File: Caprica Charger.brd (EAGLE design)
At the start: 160 x 100 mm, 60 parts, among them J1 POWER_JACKPTH, Q4 MOSFET, Q5 MOSFET

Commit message: Everything patched together
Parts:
- moved R11 20.5 mm to (8.89, 5.08)
- moved D2 16.5 mm to (12.7, 6.35), turned to 0 degrees
- moved R13 11.7 mm to (21.6, 5.08)
- moved U$5 10.8 mm to (5.71, 11.3), turned to 0 degrees
- moved D4 8.89 mm to (24.1, 6.35), turned to 0 degrees
- moved R12 8.03 mm to (29.2, 5.08)
- moved D3 2.54 mm to (34.3, 6.35), turned to 0 degrees
- moved R10 1.67 mm to (19.4, 9.40), turned to 180 degrees
- moved R9 0.25 mm to (21.1, 11.8)
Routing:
- net VIN: track 42.2 -> 61.3 mm
- net N$10: track 12.7 -> 29.6 mm, vias 0 -> 2
- net THERM: track 6.38 -> 19.2 mm
- net N$12: track 8.86 -> 16.1 mm
- net N$13: track 1.57 -> 3.62 mm
- net N$11: track 7.00 -> 8.67 mm
- net N$1: track 1.57 -> 2.37 mm
- net GND: vias 18 -> 19
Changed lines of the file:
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@@
 <layer number="23" name="tOrigins" color="15" fill="1" visible="yes" active="yes"/>
 <layer number="24" name="bOrigins" color="15" fill="1" visible="yes" active="yes"/>
-<layer number="25" name="tNames" color="7" fill="1" visible="yes" active="yes"/>
-<layer number="26" name="bNames" color="7" fill="1" visible="yes" active="yes"/>
-<layer number="27" name="tValues" color="7" fill="1" visible="yes" active="yes"/>
-<layer number="28" name="bValues" color="7" fill="1" visible="yes" active="yes"/>
+<layer number="25" name="tNames" color="7" fill="1" visible="no" active="yes"/>
+<layer number="26" name="bNames" color="7" fill="1" visible="no" active="yes"/>
+<layer number="27" name="tValues" color="7" fill="1" visible="no" active="yes"/>
+<layer number="28" name="bValues" color="7" fill="1" visible="no" active="yes"/>
 <layer number="29" name="tStop" color="7" fill="3" visible="no" active="yes"/>
 <layer number="30" name="bStop" color="7" fill="6" visible="no" active="yes"/>
@@
 <element name="C9" library="SparkFun" package="1206" value="10uF" x="55.88" y="6.35" rot="R270"/>
 <element name="C4" library="SparkFun" package="1206" value="2.2uF" x="39.37" y="5.08" rot="R90"/>
-<element name="D2" library="SparkFun" package="LED-1206" value="" x="29.21" y="6.35" rot="R90"/>
-<element name="D3" library="SparkFun" package="LED-1206" value="" x="36.83" y="6.35" rot="R90"/>
-<element name="D4" library="SparkFun" package="LED-1206" value="" x="33.02" y="6.35" rot="R90"/>
-<element name="R11" library="Taylor" package="0603-RES" value="100k" x="29.21" y="2.54" rot="R270"/>
-<element name="R12" library="Taylor" package="0603-RES" value="100k" x="36.83" y="2.54" rot="R270"/>
-<element name="R13" library="Taylor" package="0603-RES" value="100k" x="33.02" y="2.54" rot="R270"/>
+<element name="D2" library="SparkFun" package="LED-1206" value="" x="12.7" y="6.35"/>
+<element name="D3" library="SparkFun" package="LED-1206" value="" x="34.29" y="6.35"/>
+<element name="D4" library="SparkFun" package="LED-1206" value="" x="24.13" y="6.35"/>
+<element name="R11" library="Taylor" package="0603-RES" value="100k" x="8.89" y="5.08" rot="R270"/>
+<element name="R12" library="Taylor" package="0603-RES" value="100k" x="29.21" y="5.08" rot="R270"/>
+<element name="R13" library="Taylor" package="0603-RES" value="100k" x="21.59" y="5.08" rot="R270"/>
 <element name="C1" library="Taylor" package="0603-CAP" value="0.1uF" x="24.13" y="9.525" rot="R90"/>
 <element name="R16" library="Taylor" package="0603-RES" value="100k" x="21.082" y="10.414" rot="R180"/>
-<element name="R9" library="Taylor" package="0603-RES" value="9.31k" x="21.082" y="11.557" rot="R180"/>
-<element name="R10" library="Taylor" package="0603-RES" value="430k" x="21.082" y="9.144"/>
+<element name="R9" library="Taylor" package="0603-RES" value="9.31k" x="21.082" y="11.811" rot="R180"/>
+<element name="R10" library="Taylor" package="0603-RES" value="430k" x="19.431" y="9.398" rot="R180"/>
 <element name="CTTC" library="Taylor" package="0603-CAP" value="0.056uF" x="35.56" y="12.7" rot="R180"/>
 <element name="R7" library="Taylor" package="0603-RES" value="100k" x="43.18" y="3.81" rot="R180"/>
@@
 <element name="C19" library="SparkFun" package="1206" value="10uF" x="29.21" y="25.4" rot="R90"/>
 <element name="C20" library="SparkFun" package="1206" value="10uF" x="26.67" y="25.4" rot="R90"/>
-<element name="U$5" library="Taylor" package="DF13-2" value="DF13-2HORIZONTAL" x="16.383" y="9.525" rot="R270"/>
+<element name="U$5" library="Taylor" package="DF13-2" value="DF13-2HORIZONTAL" x="5.715" y="11.303"/>
 </elements>
 <signals>
@@
 <via x="41.148" y="7.747" extent="1-16" drill="0.4064"/>
 <wire x1="38.1" y1="16.51" x2="37.465" y2="15.875" width="0.254" layer="1"/>
+<via x="43.688" y="18.415" extent="1-16" drill="0.4064"/>
 </signal>
 <signal name="VIN">
@@
 <vertex x="16.383" y="19.304"/>
 </polygon>
-<wire x1="33.02" y1="1.8" x2="36.83" y2="1.8" width="0.4064" layer="1"/>
-<wire x1="36.83" y1="1.8" x2="29.21" y2="1.8" width="0.4064" layer="1"/>
+<wire x1="21.59" y1="4.34" x2="29.21" y2="4.34" width="0.4064" layer="1"/>
+<wire x1="29.21" y1="4.34" x2="8.89" y2="4.34" width="0.4064" layer="1"/>
 <wire x1="17.04" y1="25.4" x2="16.51" y2="24.87" width="0.6096" layer="1"/>
 <wire x1="16.51" y1="24.87" x2="16.51" y2="22.86" width="0.6096" layer="1"/>
-<wire x1="29.21" y1="1.8" x2="26.14" y2="1.8" width="0.4064" layer="1"/>
-<wire x1="26.14" y1="1.8" x2="21.59" y2="6.35" width="0.4064" layer="1"/>
-<via x="21.59" y="6.35" extent="1-16" drill="0.4064"/>
-<wire x1="21.59" y1="6.35" x2="21.59" y2="8.89" width="0.4064" layer="16"/>
-<wire x1="21.59" y1="8.89" x2="15.24" y2="15.24" width="0.4064" layer="16"/>
+<wire x1="8.89" y1="4.34" x2="19.79" y2="4.34" width="0.4064" layer="1"/>
+<wire x1="19.79" y1="4.34" x2="20.32" y2="7.62" width="0.4064" layer="1"/>
+<via x="20.32" y="7.62" extent="1-16" drill="0.4064"/>
+<wire x1="20.32" y1="7.62" x2="20.32" y2="8.89" width="0.4064" layer="16"/>
+<wire x1="20.32" y1="8.89" x2="15.24" y2="15.24" width="0.4064" layer="16"/>
 <wire x1="15.24" y1="15.24" x2="15.24" y2="17.78" width="0.4064" layer="16"/>
 <wire x1="15.24" y1="17.78" x2="13.7" y2="19.32" width="0.4064" layer="16"/>
@@
 <via x="30.607" y="14.351" extent="1-16" drill="0.4064"/>
 <wire x1="30.607" y1="14.351" x2="30.607" y2="14.986" width="0.254" layer="1"/>
-<wire x1="21.822" y1="11.557" x2="22.584" y2="11.557" width="0.4064" layer="1"/>
+<wire x1="21.822" y1="11.811" x2="22.584" y2="11.557" width="0.4064" layer="1"/>
 <wire x1="22.584" y1="11.557" x2="22.987" y2="11.938" width="0.4064" layer="1"/>
 <via x="22.987" y="11.938" extent="1-16" drill="0.4064"/>
@@
 <contactref element="D2" pad="A"/>
 <contactref element="R11" pad="1"/>
-<wire x1="29.21" y1="4.85" x2="29.21" y2="3.28" width="0.4064" layer="1"/>
+<wire x1="11.2" y1="6.35" x2="8.89" y2="5.82" width="0.4064" layer="1"/>
 </signal>
 <signal name="N$10">
@@
 <wire x1="33.528" y1="15.24" x2="32.131" y2="15.24" width="0.254" layer="1"/>
 <wire x1="32.131" y1="15.24" x2="31.75" y2="14.859" width="0.254" layer="1"/>
-<wire x1="29.21" y1="7.85" x2="29.21" y2="11.43" width="0.254" layer="1"/>
 <wire x1="29.21" y1="11.43" x2="31.75" y2="13.97" width="0.254" layer="1"/>
 <wire x1="31.75" y1="13.97" x2="31.75" y2="14.859" width="0.254" layer="1"/>
+<wire x1="29.21" y1="11.43" x2="27.94" y2="10.16" width="0.3048" layer="1"/>
+<wire x1="27.94" y1="10.16" x2="27.94" y2="8.89" width="0.3048" layer="1"/>
+<via x="27.94" y="8.89" extent="1-16" drill="0.4064"/>
+<via x="16.51" y="8.89" extent="1-16" drill="0.4064"/>
+<wire x1="16.51" y1="8.89" x2="13.97" y2="6.35" width="0.3048" layer="1"/>
+<wire x1="14.2" y1="6.35" x2="13.97" y2="6.35" width="0.3048" layer="1"/>
+<wire x1="27.94" y1="8.89" x2="25.4" y2="6.35" width="0.3048" layer="16"/>
+<wire x1="25.4" y1="6.35" x2="19.05" y2="6.35" width="0.3048" layer="16"/>
+<wire x1="19.05" y1="6.35" x2="16.51" y2="8.89" width="0.3048" layer="16"/>
 </signal>
 <signal name="N$11">
@@
 <wire x1="37.85" y1="14.46" x2="37.85" y2="10.664" width="0.254" layer="1"/>
 <wire x1="37.85" y1="10.664" x2="37.846" y2="10.541" width="0.254" layer="1"/>
-<wire x1="36.83" y1="7.85" x2="36.83" y2="9.398" width="0.254" layer="1"/>
+<wire x1="35.79" y1="6.35" x2="36.83" y2="9.398" width="0.254" layer="1"/>
 <wire x1="36.83" y1="9.398" x2="37.846" y2="10.541" width="0.254" layer="1"/>
 </signal>
@@
 <wire x1="37.338" y1="14.448" x2="37.338" y2="11.938" width="0.254" layer="1"/>
 <wire x1="37.338" y1="11.938" x2="33.02" y2="7.62" width="0.254" layer="1"/>
-<wire x1="33.02" y1="7.62" x2="33.02" y2="7.85" width="0.254" layer="1"/>
+<wire x1="33.02" y1="7.62" x2="25.63" y2="6.35" width="0.254" layer="1"/>
 </signal>
 <signal name="N$13">
 <contactref element="D3" pad="A"/>
 <contactref element="R12" pad="1"/>
-<wire x1="36.83" y1="4.85" x2="36.83" y2="3.28" width="0.4064" layer="1"/>
+<wire x1="32.79" y1="6.35" x2="29.21" y2="5.82" width="0.4064" layer="1"/>
 </signal>
 <signal name="N$14">
 <contactref element="D4" pad="A"/>
 <contactref element="R13" pad="1"/>
-<wire x1="33.02" y1="4.85" x2="33.02" y2="3.28" width="0.4064" layer="1"/>
+<wire x1="22.63" y1="6.35" x2="21.59" y2="5.82" width="0.4064" layer="1"/>
 </signal>
 <signal name="THERM">
@@
 <contactref element="R16" pad="2"/>
 <contactref element="U$5" pad="P1"/>
-<wire x1="20.342" y1="11.557" x2="20.342" y2="10.414" width="0.6096" layer="1"/>
-<wire x1="20.342" y1="10.414" x2="20.342" y2="9.144" width="0.6096" layer="1"/>
-<wire x1="20.342" y1="11.557" x2="18.934" y2="11.695" width="0.4064" layer="1"/>
-<wire x1="18.934" y1="11.695" x2="16.383" y2="11.695" width="0.4064" layer="1"/>
+<wire x1="20.342" y1="11.811" x2="20.342" y2="10.414" width="0.6096" layer="1"/>
+<wire x1="20.342" y1="10.414" x2="20.171" y2="9.398" width="0.6096" layer="1"/>
+<wire x1="20.342" y1="11.811" x2="18.934" y2="11.695" width="0.4064" layer="1"/>
+<wire x1="18.934" y1="11.695" x2="3.545" y2="11.303" width="0.4064" layer="1"/>
 </signal>
 <signal name="N$18">

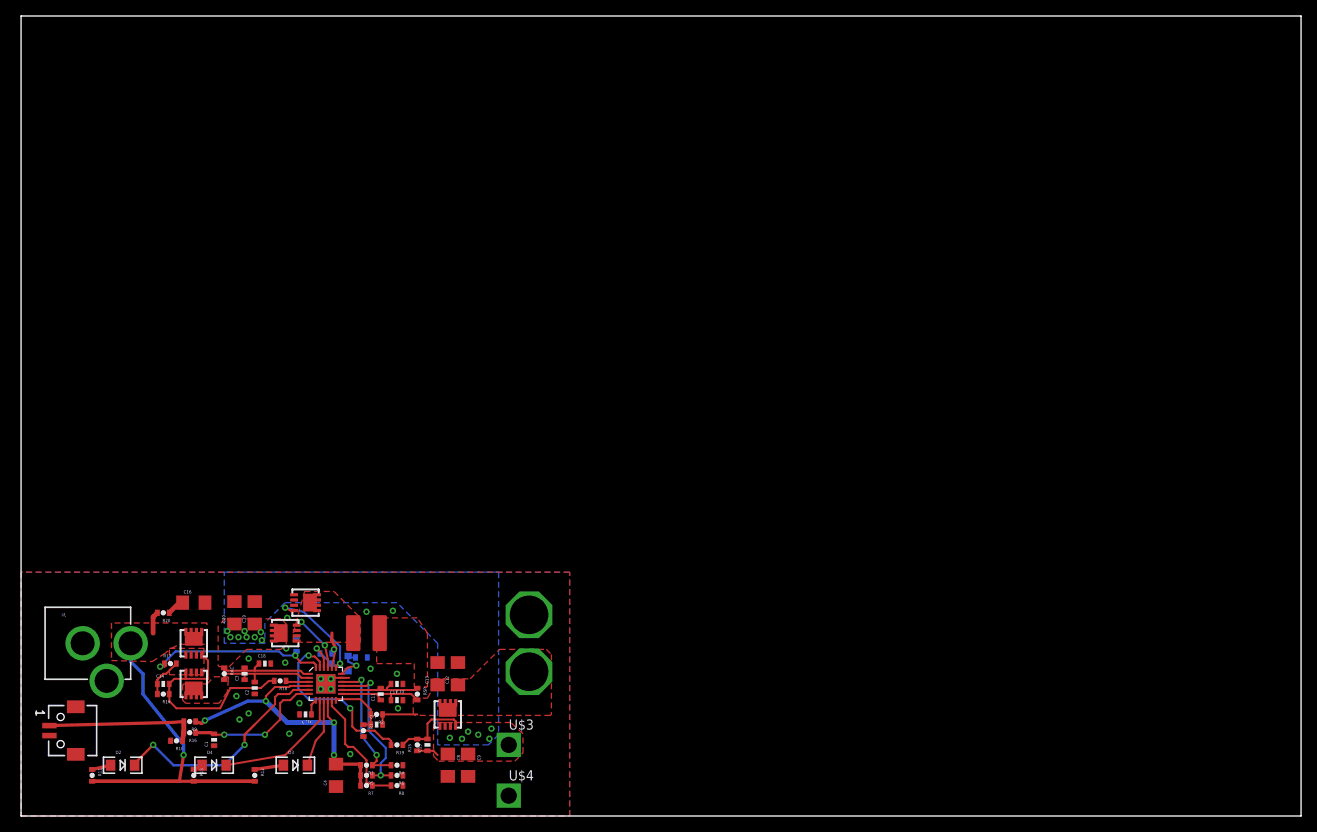
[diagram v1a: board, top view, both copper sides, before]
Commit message: Balancing added and all laid out. Still may be all wrong.
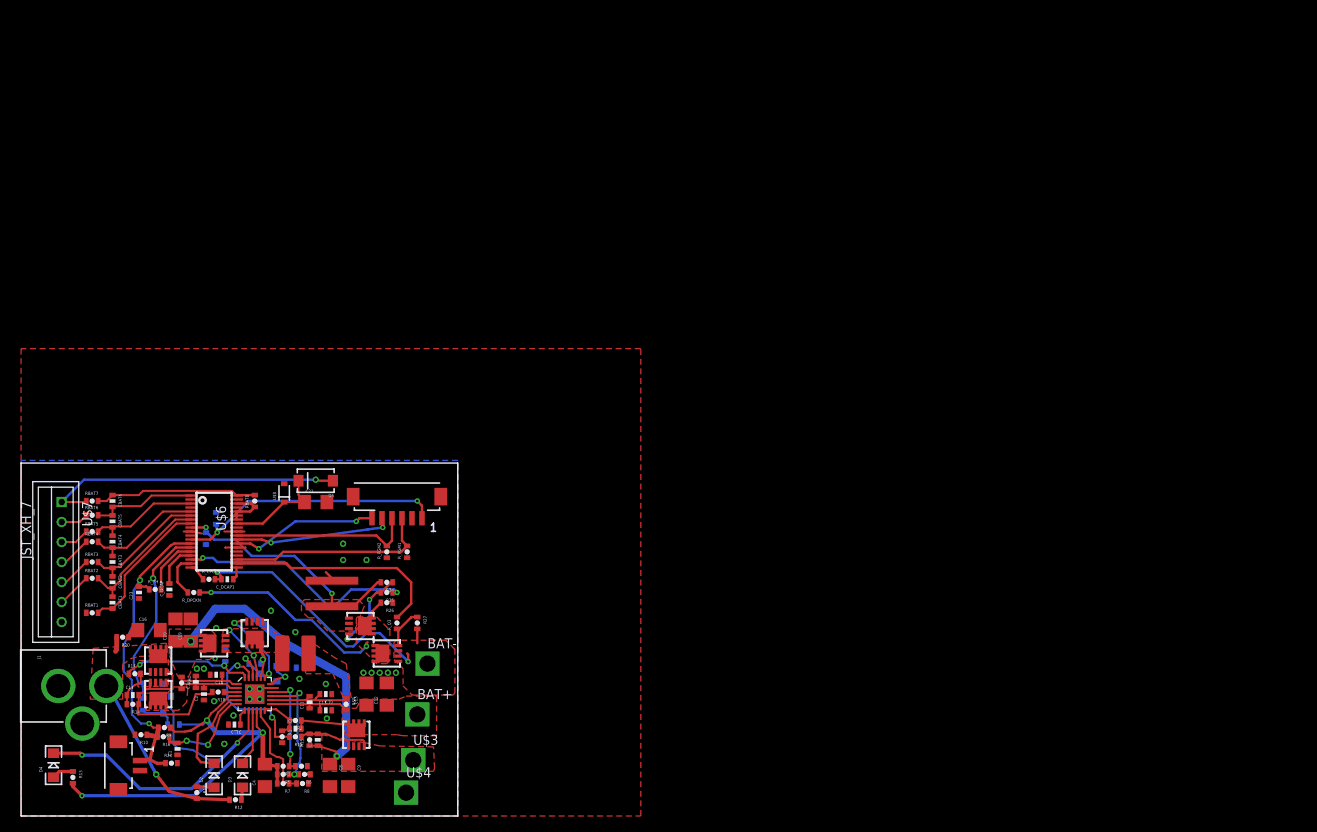
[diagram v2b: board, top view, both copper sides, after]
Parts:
- removed U$5: DF13-2HORIZONTAL, Taylor:DF13-2
- added BAT+, BAT-: HIGHCURRENTPAD2, Taylor:HIGH_CURRENT_PAD2
- added C21: 10uF, SparkFun:1206
- added C22, C23, CS-: 0.1uF, Taylor:0603-CAP
- added CBAT1, CBAT2, CBAT3, CBAT4, CBAT5, CBAT6, C_DCAP, C_DCAP1: 1uF, Taylor:0603-CAP
- added D5: (no value), SparkFun:SMA-DIODE
- added D7: (no value), SparkFun:SOD-323
- added Q6, Q7: MOSFET, Taylor:POWERPAK_1212-8
- added Q8: MOSFET-NCHANNELSMD, SparkFun:SOT23-3
- added R21: THERM, Taylor:0603-RES
- added R22: (no value), Taylor:OHMITE_FCSL64_CURRENT_SENSE_RESISTOR
- added R23, R_TH: 100k, Taylor:0603-RES
- added R24, R27: 5.1M, Taylor:0603-RES
- added R25, R_CHG_DET, R_PGM1, R_PGM2, R_Q3: 1k, Taylor:0603-RES
- added R26: 47k, Taylor:0603-RES
- added RBAT1, RBAT2, RBAT3, RBAT4, RBAT5, RBAT6, RBAT7: 50R, Taylor:0603-RES
- added RBAT8, R_CPCKN, R_DPCKN: 100R, Taylor:0603-RES
- added U$6: BQ77910A_BATTERY_PROTECTOR, Taylor:TSSOP38
- added U$7: JST_XH_7, Taylor:B7B-XH
- added U$8: DIODE-ZENER-BZT52, SparkFun:SOD-323
- added U$9: DF13-6, Taylor:DF13-6-VERT
- C7: value 0.1uF -> 1uF
- R13: value 100k -> 270R
- U$2: value XT60 -> DF13-2VERTICAL; device Taylor:XT60_CONNECTOR -> Taylor:DF13-2-VERT
- moved U$2 51.8 mm to (14.0, 6.35), turned to 180 degrees
- moved D4 20.1 mm to (4.06, 6.35), turned to 90 degrees
- moved R13 15.1 mm to (6.48, 4.83)
- moved C9 15.0 mm to (40.9, 5.08)
- moved C8 14.8 mm to (38.6, 5.08)
- moved C15 13.7 mm to (37.1, 9.53)
- moved R15 13.5 mm to (36.1, 9.53)
- moved R11 13.3 mm to (22.0, 2.92)
- moved U$4 12.8 mm to (48.1, 2.92)
- moved R19 12.7 mm to (34.3, 9.91)
- moved U$3 12.1 mm to (49.0, 6.99)
- moved R4 11.9 mm to (35.1, 6.22)
- moved R8 11.8 mm to (35.2, 4.06)
- moved Q3 11.7 mm to (41.9, 10.2)
- moved R6 11.6 mm to (35.4, 5.21)
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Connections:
- net N$22 renamed HIDRV
- net SYS renamed SYS+
- removed net BAT: C11.1, C12.1, C13.1, C17.1, CFF.2, Q3.P5, Q3.P6, Q3.P7, Q3.P8, Q3.PAD, R2.1, RSR.2, U$1.13, U$2.P$1
- removed net THERM: R10.1, R16.2, R9.2, U$5.P1
- new net BAT+: BAT+.P$1, C11.1, C12.1, C13.1, C17.1, CFF.2, D5.A, Q3.P5, Q3.P6, Q3.P7, Q3.P8, Q3.PAD, R2.1, RBAT7.1, RSR.2, U$1.13, U$7.P$1
- new net BAT-: BAT-.P$1, C_DCAP1.2, Q7.P1, Q7.P2, Q7.P3, R27.2, R_CPCKN.2
- new net CHG_DET: Q8.3, R23.2, R_CHG_DET.2
- new net N$17: CBAT2.1, CBAT3.2, RBAT3.2, U$6.6
- new net N$22: CBAT3.1, CBAT4.2, RBAT4.2, U$6.5
- new net N$23: CBAT1.2, RBAT1.2, U$6.8
- new net N$29: CBAT5.1, CBAT6.2, RBAT6.2, U$6.1
- new net N$31: CBAT4.1, CBAT5.2, RBAT5.2, U$6.3
- new net N$32: C_DCAP.2, U$6.16
- new net N$33: CBAT6.1, RBAT7.2, RBAT8.2, U$6.38
- new net N$34: RBAT8.1, U$6.32, U$6.33, U$6.34, U$6.36
- new net N$35: C21.1, D5.C, U$6.31, U$8.1
- new net N$37: D7.1, R_CHG_DET.1, U$6.14
- new net N$38: RBAT2.1, U$7.P$6
- new net N$39: RBAT3.1, U$7.P$5
- new net N$40: RBAT4.1, U$7.P$4
- new net N$41: Q6.P4, R24.1, R25.2
- new net N$42: RBAT6.1, U$7.P$2
- new net N$43: RBAT5.1, U$7.P$3
- new net N$44: R_DPCKN.2, U$6.18
- new net N$46: Q6.P5, Q6.P6, Q6.P7, Q6.P8, Q6.PAD, Q7.P5, Q7.P6, Q7.P7, Q7.P8, Q7.PAD, R26.2, R_DPCKN.1
- new net N$47: U$6.27, U$9.P5
- new net N$48: CS-.1, Q6.P1, Q6.P2, Q6.P3, R22.P$1, R24.2, U$6.9
- new net N$49: C_DCAP1.1, U$6.20
- new net N$5: CBAT1.1, CBAT2.2, RBAT2.2, U$6.7
- new net N$50: R_Q3.2, U$6.21
- new net N$51: Q7.P4, R27.1, R_Q3.1
- new net N$52: U$6.26, U$9.P6
- new net N$53: R_CPCKN.1, U$6.19
- new net N$54: R_PGM2.2, U$6.28, U$9.P4
- new net N$55: R_TH.2, U$6.15
- new net N$57: R_PGM1.2, U$6.22, U$9.P3
- new net PG: D4.C, Q8.1, U$1.8
- new net TS: C23.2, R10.1, R16.2, R21.1, R9.2, R_TH.1, U$2.P1, U$6.13
- new net VREG: C22.2, U$6.12, U$9.P1
- net 3VREF: now also R13.2, R23.1
- net GND: now also C21.2, C22.1, C23.1, CS-.2, C_DCAP.1, D7.2, Q8.2, R21.2, R22.P$2, R26.1, RBAT1.1, R_PGM1.1, R_PGM2.1, U$2.P2, U$6.10, U$6.11, U$6.23, U$6.24, U$6.25, U$6.29, U$7.P$7, U$8.2, U$9.P2; no longer U$2.P$2, U$5.P2
- net N$12: now also R25.1, U$6.17; no longer D4.C, U$1.8
- net VIN: no longer R13.2
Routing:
- net BAT+: track 0.00 -> 56.0 mm, vias 0 -> 1
- net PG: track 0.00 -> 45.2 mm, vias 0 -> 2
- net TS: track 0.00 -> 42.6 mm, vias 0 -> 2
- net VIN: track 61.3 -> 24.9 mm
- net BAT-: track 0.00 -> 34.7 mm, vias 0 -> 2
- net SYS+: track 15.4 -> 49.8 mm, vias 14 -> 2
- net VREG: track 0.00 -> 33.6 mm, vias 0 -> 2
- net N$50: track 0.00 -> 27.9 mm
- net N$46: track 0.00 -> 27.2 mm, vias 0 -> 2
- net N$48: track 0.00 -> 26.8 mm, vias 0 -> 2
- net N$57: track 0.00 -> 25.8 mm
- net N$37: track 0.00 -> 23.7 mm, vias 0 -> 1
- net N$54: track 0.00 -> 23.1 mm
- net 3VREF: track 39.8 -> 61.1 mm, vias 4 -> 3
- net N$33: track 0.00 -> 20.4 mm
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- added copper zone on layer 1, net BAT+
- added copper zone on layer 1, net BAT-
- added copper zone on layer 1, net N$46
- added copper zone on layer 1, net N$48
- removed copper zone on layer 1, net BAT
- removed copper zone on layer 16, net SYS+
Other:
- board size 160 x 100 mm -> 54.6 x 44.1 mm
